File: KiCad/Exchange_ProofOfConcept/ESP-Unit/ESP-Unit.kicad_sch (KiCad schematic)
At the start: 52 parts, among them IC1 MT8870DE, J1 Jack-DC, J2 Conn_02x05_Top_Bottom, J3 Conn_01x07, U1 ESP32_NODEMCU, U2 LM317_TO-220, U3 LM358PE3, U4 TXS0108EPWR, U5 TXS0108EPWR, Y1 3.579546

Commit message: deleted:    KiCad/Exchange_ProofOfConcept/ESP-Unit/ESP-Unit-backups/ESP-Unit-2024-10-22_204833.zip 	new file:   KiCad/Exchange_ProofOfConcept/ESP-Unit/ESP-Unit-backups/ESP-Unit-2025-01-21_222447.zip 	new file:   KiCad/Exchange_ProofOfConcept/ESP-Unit/ESP-Unit-backups/ESP-Unit-2025-01-23_205217.zip 	new file:   KiCad/Exchange_ProofOfConcept/ESP-Unit/ESP-Unit-backups/ESP-Unit-2025-01-23_211741.zip 	new file:   KiCad/Exchange_ProofOfConcept/ESP-Unit/ESP-Unit-backups/ESP-Unit-2025-01-26_102636.zip 	new file:   KiCad/Exchange_ProofOfConcept/ESP-Unit/ESP-Unit-backups/ESP-Unit-2025-01-30_220613.zip 	new file:   KiCad/Exchange_ProofOfConcept/ESP-Unit/ESP-Unit-backups/ESP-Unit-2025-01-30_221846.zip 	modified:   KiCad/Exchange_ProofOfConcept/ESP-Unit/ESP-Unit.kicad_pcb 	modified:   KiCad/Exchange_ProofOfConcept/ESP-Unit/ESP-Unit.kicad_pro 	modified:   KiCad/Exchange_ProofOfConcept/ESP-Unit/ESP-Unit.kicad_sch 	modified:   KiCad/Exchange_ProofOfConcept/ESP-Unit/fp-info-cache 	deleted:    KiCad/Exchange_ProofOfConcept/Exchange_ProofOfConcept-backups/Exchange_ProofOfConcept-2024-11-20_224852.zip 	deleted:    KiCad/Exchange_ProofOfConcept/Exchange_ProofOfConcept-backups/Exchange_ProofOfConcept-2024-11-20_230009.zip 	deleted:    KiCad/Exchange_ProofOfConcept/Exchange_ProofOfConcept-backups/Exchange_ProofOfConcept-2024-11-20_231023.zip 	deleted:    KiCad/Exchange_ProofOfConcept/Exchange_ProofOfConcept-backups/Exchange_ProofOfConcept-2024-11-20_231736.zip 	new file:   KiCad/Exchange_ProofOfConcept/Exchange_ProofOfConcept-backups/Exchange_ProofOfConcept-2025-01-21_210113.zip 	new file:   KiCad/Exchange_ProofOfConcept/Exchange_ProofOfConcept-backups/Exchange_ProofOfConcept-2025-01-21_210624.zip 	new file:   KiCad/Exchange_ProofOfConcept/Exchange_ProofOfConcept-backups/Exchange_ProofOfConcept-2025-01-21_214958.zip 	new file:   KiCad/Exchange_ProofOfConcept/Exchange_ProofOfConcept-backups/Exchange_ProofOfConcept-2025-01-21_222119.zip 	deleted:    KiCad/Exchange_ProofOfConcept/Exchange_Pr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
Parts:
- removed C9: 0,1uF, Capacitor_THT:C_Disc_D5.0mm_W2.5mm_P2.50mm, symbol Device:C
- removed U4, U5: TXS0108EPWR, TSSOP-20_4.4x5mm_P0.5mm, symbol JW_library_sym:TXS0108EPWR
- added C11: 0,1uF, Capacitor_THT:C_Disc_D5.0mm_W2.5mm_P2.50mm, symbol Device:C
- added U4, U5: BOB-12009, JW_footprint_library:CONV_BOB-12009, symbol JW_library_sym:BOB-12009
- gave numbers to parts that had none: 1
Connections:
- net 3V3: now also U4.LV, U5.LV
- net 5V: now also C11.2, U4.HV, U5.HV
- net Earth: now also C11.1, U4.GND_1 (GND), U4.GND_2 (GND), U5.GND_1 (GND), U5.GND_2 (GND)
- net MCP_RESET: now also U4.HV4
- net MCP_RESET_3V: now also U4.LV4
- net Q1_3V: now also U5.LV4
- net Q2_3V: now also U5.LV3
- net Q3_3V: now also U5.LV2
- net Q4_3V: now also U5.LV1
- net SCL_3V: now also U4.LV2
- net SDA: now also U4.HV1
- net SDA_3V: now also U4.LV1
- net SLC: now also U4.HV2
- net SLIC_INT: now also U4.HV3
- net SLIC_INT_3V: now also U4.LV3
- net at IC1.11 (Q1): now also U5.HV4
- net at IC1.12 (Q2): now also U5.HV3
- net at IC1.13 (Q3): now also U5.HV2
- net at IC1.14 (Q4): now also U5.HV1
- net MT8870_PWDN: no longer names the net of IC1.6 (PWDN)
- net MT8870_PWDN_3V: no longer names the net of U1.J5_12 (G33)
- no-connect marks 30 -> 17
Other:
- moved on the sheet: C8

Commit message: modified:   KiCad/Exchange_ProofOfConcept/ESP-Unit/ESP-Unit.kicad_sch 	deleted:    KiCad/Exchange_ProofOfConcept/ESP-Unit/_autosave-ESP-Unit.kicad_sch 	modified:   include/config.h 	new file:   include/toneHandler.h 	modified:   lib/MT8816/MT8816.cpp 	modified:   src/config.cpp 	modified:   src/hookChange.cpp 	modified:   src/lineAction.cpp 	modified:   src/main.cpp 	new file:   src/toneHandler.cpp
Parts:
- removed D2: LED, LED_THT:LED_D3.0mm, symbol Device:LED
- added R?: 47K, Resistor_THT:R_Axial_DIN0207_L6.3mm_D2.5mm_P2.54mm_Vertical, symbol Device:R
- R11: value 100K -> 22K
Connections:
- net Earth: now also R?.1
- net Q1_3V: now also U1.J5_10 (G26); no longer U1.J4_14 (G0)
- net Q2_3V: now also U1.J5_13 (G32); no longer U1.J4_15 (G2)
- net STD: now reaches R11.2
- net STD: now also U1.J5_12 (G33), R?.2
- no-connect marks 17 -> 16
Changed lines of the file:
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@@
 	)
 	(junction
+		(at 156.21 128.27)
+		(diameter 0)
+		(color 0 0 0 0)
+	)
+	(junction
 		(at 39.37 170.18)
 		(diameter 0)
@@
 	)
 	(junction
-		(at 171.45 128.27)
+		(at 167.64 123.19)
 		(diameter 0)
 		(color 0 0 0 0)
@@
 	)
 	(no_connect
+		(at 38.1 125.73)
+	)
+	(no_connect
 		(at 38.1 107.95)
 	)
@@
 	)
 	(no_connect
-		(at 78.74 128.27)
-	)
-	(no_connect
 		(at 38.1 92.71)
 	)
@@
 	)
 	(no_connect
-		(at 78.74 130.81)
-	)
-	(no_connect
 		(at 269.24 151.13)
 	)
@@
 	)
 	(no_connect
+		(at 38.1 123.19)
+	)
+	(no_connect
 		(at 38.1 118.11)
 	)
@@
 		(at 78.74 92.71)
 	)
-	(no_connect
-		(at 78.74 123.19)
-	)
 	(wire
 		(pts
@@
 	(wire
 		(pts
-			(xy 160.02 123.19) (xy 158.75 123.19)
+			(xy 158.75 123.19) (xy 167.64 123.19)
 		)
 		(stroke
@@
 	(wire
 		(pts
+			(xy 167.64 128.27) (xy 167.64 123.19)
+		)
+		(stroke
+			(width 0)
+			(type default)
+		)
+	)
+	(wire
+		(pts
 			(xy 107.95 46.99) (xy 107.95 58.42)
 		)
@@
 	(wire
 		(pts
-			(xy 149.86 128.27) (xy 171.45 128.27)
+			(xy 149.86 128.27) (xy 156.21 128.27)
 		)
 		(stroke
@@
 	(wire
 		(pts
-			(xy 30.48 123.19) (xy 38.1 123.19)
-		)
-		(stroke
-			(width 0)
-			(type default)
-		)
-	)
-	(wire
-		(pts
 			(xy 39.37 175.26) (xy 39.37 177.8)
 		)
@@
 	(wire
 		(pts
-			(xy 30.48 130.81) (xy 38.1 130.81)
+			(xy 167.64 123.19) (xy 170.18 123.19)
 		)
 		(stroke
@@
 	(wire
 		(pts
-			(xy 167.64 123.19) (xy 171.45 123.19)
+			(xy 30.48 130.81) (xy 38.1 130.81)
 		)
 		(stroke
@@
 	(wire
 		(pts
+			(xy 78.74 128.27) (xy 82.55 128.27)
+		)
+		(stroke
+			(width 0)
+			(type default)
+		)
+	)
+	(wire
+		(pts
 			(xy 248.92 73.66) (xy 248.92 83.82)
 		)
@@
 	(wire
 		(pts
+			(xy 78.74 123.19) (xy 82.55 123.19)
+		)
+		(stroke
+			(width 0)
+			(type default)
+		)
+	)
+	(wire
+		(pts
 			(xy 130.81 176.53) (xy 133.35 176.53)
 		)
@@
 	(wire
 		(pts
-			(xy 171.45 128.27) (xy 171.45 138.43)
+			(xy 156.21 128.27) (xy 156.21 138.43)
 		)
 		(stroke
@@
 	(wire
 		(pts
-			(xy 171.45 123.19) (xy 171.45 128.27)
+			(xy 31.75 165.1) (xy 39.37 165.1)
 		)
 		(stroke
@@
 	(wire
 		(pts
-			(xy 31.75 165.1) (xy 39.37 165.1)
+			(xy 78.74 130.81) (xy 82.55 130.81)
 		)
 		(stroke
@@
 	(wire
 		(pts
+			(xy 156.21 128.27) (xy 160.02 128.27)
+		)
+		(stroke
+			(width 0)
+			(type default)
+		)
+	)
+	(wire
+		(pts
 			(xy 120.65 110.49) (xy 124.46 110.49)
 		)
@@
 	(wire
 		(pts
-			(xy 30.48 125.73) (xy 38.1 125.73)
-		)
-		(stroke
-			(width 0)
-			(type default)
-		)
-	)
-	(wire
-		(pts
 			(xy 74.93 50.8) (xy 83.82 50.8)
 		)
@@
 		)
 	)
+	(label "STD"
+		(at 82.55 130.81 0)
+		(effects
+			(font
+				(size 1.27 1.27)
+			)
+			(justify left bottom)
+		)
+	)
 	(label "3V3"
 		(at 92.71 85.09 0)
@@
 		)
 	)
+	(label "STD"
+		(at 170.18 123.19 0)
+		(effects
+			(font
+				(size 1.27 1.27)
+			)
+			(justify left bottom)
+		)
+	)
 	(label "5V"
 		(at 118.11 86.36 180)
@@
 		)
 	)
-	(label "Q2_3V"
-		(at 30.48 125.73 180)
-		(effects
-			(font
-				(size 1.27 1.27)
-			)
-			(justify right bottom)
-		)
-	)
 	(label "Audio_SLIC-Amp"
 		(at 81.28 167.64 0)
@@
 		)
 	)
+	(label "Q1_3V"
+		(at 82.55 123.19 0)
+		(effects
+			(font
+				(size 1.27 1.27)
+			)
+			(justify left bottom)
+		)
+	)
 	(label "3V3"
 		(at 180.34 55.88 0)
@@
 		)
 	)
+	(label "Q2_3V"
+		(at 82.55 128.27 0)
+		(effects
+			(font
+				(size 1.27 1.27)
+			)
+			(justify left bottom)
+		)
+	)
 	(label "Audio_SLIC"
 		(at 248.92 71.12 0)
@@
 		)
 	)
-	(label "Q1_3V"
-		(at 30.48 123.19 180)
-		(effects
-			(font
-				(size 1.27 1.27)
-			)
-			(justify right bottom)
-		)
-	)
 	(label "Vref"
 		(at 134.62 31.75 0)
@@
 	)
 	(symbol
+		(lib_id "Device:R")
+		(at 163.83 128.27 90)
+		(unit 1)
+		(exclude_from_sim no)
+		(in_bom yes)
+		(on_board yes)
+		(dnp no)
+		(property "Reference" "R?"
+			(at 166.624 130.302 90)
+			(effects
+				(font
+					(size 1.27 1.27)
+				)
+				(justify left)
+			)
+		)
+		(property "Value" "47K"
+			(at 166.37 128.27 90)
+			(effects
+				(font
+					(size 1.27 1.27)
+				)
+				(justify left)
+			)
+		)
+		(property "Footprint" "Resistor_THT:R_Axial_DIN0207_L6.3mm_D2.5mm_P2.54mm_Vertical"
+			(at 163.83 130.048 90)
+			(effects
+				(font
+					(size 1.27 1.27)
+				)
+				(hide yes)
+			)
+		)
+		(property "Datasheet" "~"
+			(at 163.83 128.27 0)
+			(effects
+				(font
+					(size 1.27 1.27)
+				)
+				(hide yes)
+			)
+		)
+		(property "Description" "Resistor"
+			(at 163.83 128.27 0)
+			(effects
+				(font
+					(size 1.27 1.27)
+				)
+				(hide yes)
+			)
+		)
+		(pin "2"
+		)
+		(pin "1"
+		)
+		(instances
+			(project "ESP-Unit"
+				(path "/2411d7b8-ed2d-41a6-b5ea-3554d7cee414"
+					(reference "R?")
+					(unit 1)
+				)
+			)
+		)
+	)
+	(symbol
 		(lib_id "Device:C_Polarized_US")
 		(at 30.48 85.09 0)
@@
 	(symbol
 		(lib_id "power:Earth")
-		(at 171.45 138.43 0)
+		(at 156.21 138.43 0)
 		(mirror y)
 		(unit 1)
@@
 		(fields_autoplaced yes)
 		(property "Reference" "#PWR08"
-			(at 171.45 144.78 0)
+			(at 156.21 144.78 0)
 			(effects
 				(font
@@
 		)
 		(property "Value" "Earth"
-			(at 171.45 143.51 0)
+			(at 156.21 143.51 0)
 			(effects
 				(font
@@
 		)
 		(property "Footprint" ""
-			(at 171.45 138.43 0)
+			(at 156.21 138.43 0)
 			(effects
 				(font
@@
 		)
 		(property "Datasheet" "~"
-			(at 171.45 138.43 0)
+			(at 156.21 138.43 0)
 			(effects
 				(font
@@
 		)
 		(property "Description" "Power symbol creates a global label with name \"Earth\""
-			(at 171.45 138.43 0)
+			(at 156.21 138.43 0)
 			(effects
 				(font
@@
 	)
 	(symbol
-		(lib_id "Device:LED")
-		(at 163.83 123.19 180)
-		(unit 1)
-		(exclude_from_sim no)
-		(in_bom yes)
-		(on_board yes)
-		(dnp no)
-		(property "Reference" "D2"
-			(at 163.322 120.396 0)
-			(effects
-				(font
-					(size 1.27 1.27)
-				)
-			)
-		)
-		(property "Value" "LED"
-			(at 163.83 125.984 0)
-			(effects
-				(font
-					(size 1.27 1.27)
-				)
-			)
-		)
-		(property "Footprint" "LED_THT:LED_D3.0mm"
-			(at 163.83 123.19 0)
-			(effects
-				(font
-					(size 1.27 1.27)
-				)
-				(hide yes)
-			)
-		)
-		(property "Datasheet" "~"
-			(at 163.83 123.19 0)
-			(effects
-				(font
-					(size 1.27 1.27)
-				)
-				(hide yes)
-			)
-		)
-		(property "Description" "Light emitting diode"
-			(at 163.83 123.19 0)
-			(effects
-				(font
-					(size 1.27 1.27)
-				)
-				(hide yes)
-			)
-		)
-		(pin "1"
-		)
-		(pin "2"
-		)
-		(instances
-			(project "ESP-Unit"
-				(path "/2411d7b8-ed2d-41a6-b5ea-3554d7cee414"
-					(reference "D2")
-					(unit 1)
-				)
-			)
-		)
-	)
-	(symbol
 		(lib_id "Device:R")
 		(at 154.94 123.19 90)
@@
 			)
 		)
-		(property "Value" "100K"
+		(property "Value" "22K"
 			(at 157.48 123.19 90)
 			(effects

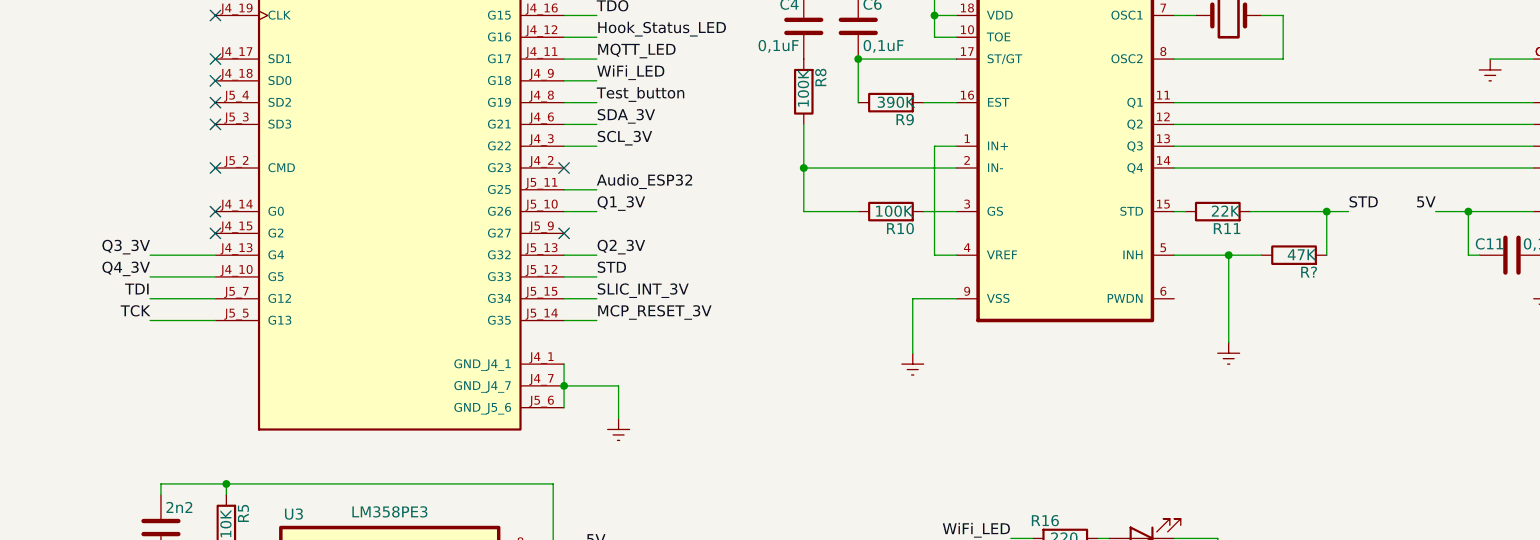
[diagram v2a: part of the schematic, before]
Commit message: Revert "Number dailing"
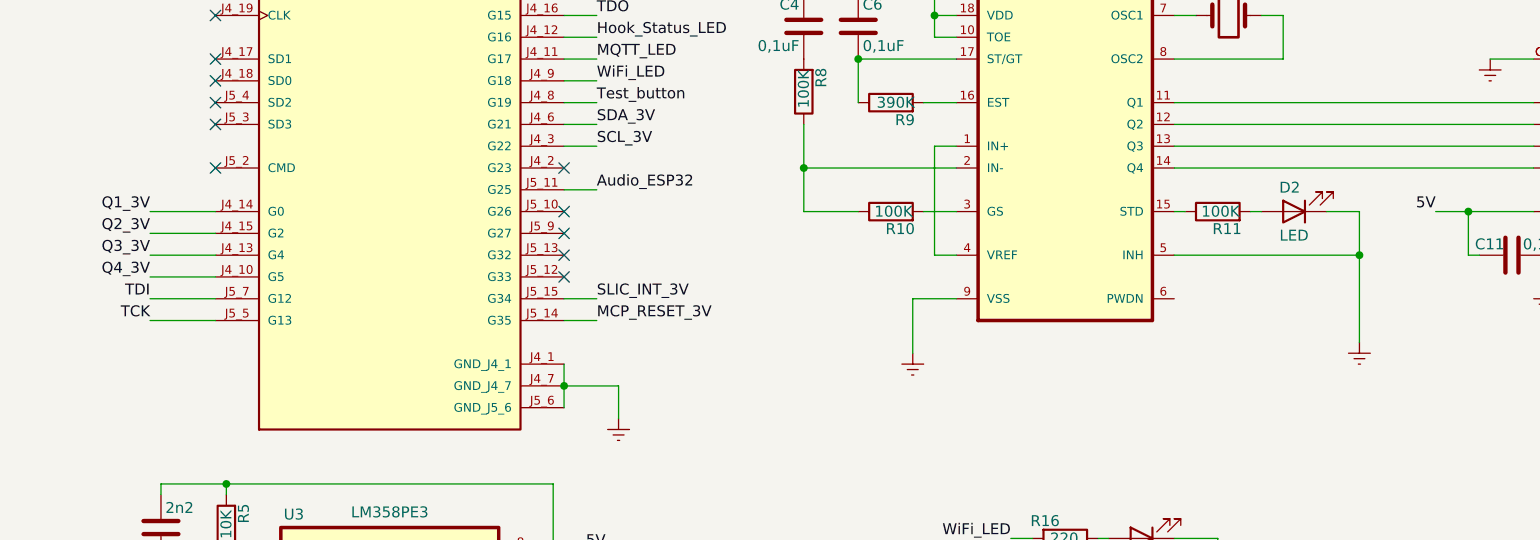
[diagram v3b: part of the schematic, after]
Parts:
- removed R?: 47K, Resistor_THT:R_Axial_DIN0207_L6.3mm_D2.5mm_P2.54mm_Vertical, symbol Device:R
- added D2: LED, LED_THT:LED_D3.0mm, symbol Device:LED
- R11: value 22K -> 100K
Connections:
- net Earth: now also D2.1 (K)
- net Q1_3V: now also U1.J4_14 (G0); no longer U1.J5_10 (G26)
- net Q2_3V: now also U1.J4_15 (G2); no longer U1.J5_13 (G32)
- net STD: no longer names the net of R11.2
- net STD: now also D2.2 (A); no longer U1.J5_12 (G33)
- no-connect marks 16 -> 17
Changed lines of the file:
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@@
 	)
 	(junction
-		(at 156.21 128.27)
-		(diameter 0)
-		(color 0 0 0 0)
-	)
-	(junction
 		(at 39.37 170.18)
 		(diameter 0)
@@
 	)
 	(junction
-		(at 167.64 123.19)
+		(at 171.45 128.27)
 		(diameter 0)
 		(color 0 0 0 0)
@@
 	)
 	(no_connect
-		(at 38.1 125.73)
-	)
-	(no_connect
 		(at 38.1 107.95)
 	)
@@
 	)
 	(no_connect
+		(at 78.74 128.27)
+	)
+	(no_connect
 		(at 38.1 92.71)
 	)
@@
 	)
 	(no_connect
+		(at 78.74 130.81)
+	)
+	(no_connect
 		(at 269.24 151.13)
 	)
@@
 	)
 	(no_connect
-		(at 38.1 123.19)
-	)
-	(no_connect
 		(at 38.1 118.11)
 	)
@@
 		(at 78.74 92.71)
 	)
+	(no_connect
+		(at 78.74 123.19)
+	)
 	(wire
 		(pts
@@
 	(wire
 		(pts
-			(xy 158.75 123.19) (xy 167.64 123.19)
+			(xy 160.02 123.19) (xy 158.75 123.19)
 		)
 		(stroke
@@
 	(wire
 		(pts
-			(xy 167.64 128.27) (xy 167.64 123.19)
-		)
-		(stroke
-			(width 0)
-			(type default)
-		)
-	)
-	(wire
-		(pts
 			(xy 107.95 46.99) (xy 107.95 58.42)
 		)
@@
 	(wire
 		(pts
-			(xy 149.86 128.27) (xy 156.21 128.27)
+			(xy 149.86 128.27) (xy 171.45 128.27)
 		)
 		(stroke
@@
 	(wire
 		(pts
+			(xy 30.48 123.19) (xy 38.1 123.19)
+		)
+		(stroke
+			(width 0)
+			(type default)
+		)
+	)
+	(wire
+		(pts
 			(xy 39.37 175.26) (xy 39.37 177.8)
 		)
@@
 	(wire
 		(pts
-			(xy 167.64 123.19) (xy 170.18 123.19)
+			(xy 30.48 130.81) (xy 38.1 130.81)
 		)
 		(stroke
@@
 	(wire
 		(pts
-			(xy 30.48 130.81) (xy 38.1 130.81)
+			(xy 167.64 123.19) (xy 171.45 123.19)
 		)
 		(stroke
@@
 	(wire
 		(pts
-			(xy 78.74 128.27) (xy 82.55 128.27)
-		)
-		(stroke
-			(width 0)
-			(type default)
-		)
-	)
-	(wire
-		(pts
 			(xy 248.92 73.66) (xy 248.92 83.82)
 		)
@@
 	(wire
 		(pts
-			(xy 78.74 123.19) (xy 82.55 123.19)
-		)
-		(stroke
-			(width 0)
-			(type default)
-		)
-	)
-	(wire
-		(pts
 			(xy 130.81 176.53) (xy 133.35 176.53)
 		)
@@
 	(wire
 		(pts
-			(xy 156.21 128.27) (xy 156.21 138.43)
+			(xy 171.45 128.27) (xy 171.45 138.43)
 		)
 		(stroke
@@
 	(wire
 		(pts
-			(xy 31.75 165.1) (xy 39.37 165.1)
+			(xy 171.45 123.19) (xy 171.45 128.27)
 		)
 		(stroke
@@
 	(wire
 		(pts
-			(xy 78.74 130.81) (xy 82.55 130.81)
+			(xy 31.75 165.1) (xy 39.37 165.1)
 		)
 		(stroke
@@
 	(wire
 		(pts
-			(xy 156.21 128.27) (xy 160.02 128.27)
-		)
-		(stroke
-			(width 0)
-			(type default)
-		)
-	)
-	(wire
-		(pts
 			(xy 120.65 110.49) (xy 124.46 110.49)
 		)
@@
 	(wire
 		(pts
+			(xy 30.48 125.73) (xy 38.1 125.73)
+		)
+		(stroke
+			(width 0)
+			(type default)
+		)
+	)
+	(wire
+		(pts
 			(xy 74.93 50.8) (xy 83.82 50.8)
 		)
@@
 		)
 	)
-	(label "STD"
-		(at 82.55 130.81 0)
-		(effects
-			(font
-				(size 1.27 1.27)
-			)
-			(justify left bottom)
-		)
-	)
 	(label "3V3"
 		(at 92.71 85.09 0)
@@
 		)
 	)
-	(label "STD"
-		(at 170.18 123.19 0)
-		(effects
-			(font
-				(size 1.27 1.27)
-			)
-			(justify left bottom)
-		)
-	)
 	(label "5V"
 		(at 118.11 86.36 180)
@@
 		)
 	)
+	(label "Q2_3V"
+		(at 30.48 125.73 180)
+		(effects
+			(font
+				(size 1.27 1.27)
+			)
+			(justify right bottom)
+		)
+	)
 	(label "Audio_SLIC-Amp"
 		(at 81.28 167.64 0)
@@
 		)
 	)
-	(label "Q1_3V"
-		(at 82.55 123.19 0)
-		(effects
-			(font
-				(size 1.27 1.27)
-			)
-			(justify left bottom)
-		)
-	)
 	(label "3V3"
 		(at 180.34 55.88 0)
@@
 		)
 	)
-	(label "Q2_3V"
-		(at 82.55 128.27 0)
-		(effects
-			(font
-				(size 1.27 1.27)
-			)
-			(justify left bottom)
-		)
-	)
 	(label "Audio_SLIC"
 		(at 248.92 71.12 0)
@@
 		)
 	)
+	(label "Q1_3V"
+		(at 30.48 123.19 180)
+		(effects
+			(font
+				(size 1.27 1.27)
+			)
+			(justify right bottom)
+		)
+	)
 	(label "Vref"
 		(at 134.62 31.75 0)
@@
 	)
 	(symbol
-		(lib_id "Device:R")
-		(at 163.83 128.27 90)
-		(unit 1)
-		(exclude_from_sim no)
-		(in_bom yes)
-		(on_board yes)
-		(dnp no)
-		(property "Reference" "R?"
-			(at 166.624 130.302 90)
-			(effects
-				(font
-					(size 1.27 1.27)
-				)
-				(justify left)
-			)
-		)
-		(property "Value" "47K"
-			(at 166.37 128.27 90)
-			(effects
-				(font
-					(size 1.27 1.27)
-				)
-				(justify left)
-			)
-		)
-		(property "Footprint" "Resistor_THT:R_Axial_DIN0207_L6.3mm_D2.5mm_P2.54mm_Vertical"
-			(at 163.83 130.048 90)
-			(effects
-				(font
-					(size 1.27 1.27)
-				)
-				(hide yes)
-			)
-		)
-		(property "Datasheet" "~"
-			(at 163.83 128.27 0)
-			(effects
-				(font
-					(size 1.27 1.27)
-				)
-				(hide yes)
-			)
-		)
-		(property "Description" "Resistor"
-			(at 163.83 128.27 0)
-			(effects
-				(font
-					(size 1.27 1.27)
-				)
-				(hide yes)
-			)
-		)
-		(pin "2"
-		)
-		(pin "1"
-		)
-		(instances
-			(project "ESP-Unit"
-				(path "/2411d7b8-ed2d-41a6-b5ea-3554d7cee414"
-					(reference "R?")
-					(unit 1)
-				)
-			)
-		)
-	)
-	(symbol
 		(lib_id "Device:C_Polarized_US")
 		(at 30.48 85.09 0)
@@
 	(symbol
 		(lib_id "power:Earth")
-		(at 156.21 138.43 0)
+		(at 171.45 138.43 0)
 		(mirror y)
 		(unit 1)
@@
 		(fields_autoplaced yes)
 		(property "Reference" "#PWR08"
-			(at 156.21 144.78 0)
+			(at 171.45 144.78 0)
 			(effects
 				(font
@@
 		)
 		(property "Value" "Earth"
-			(at 156.21 143.51 0)
+			(at 171.45 143.51 0)
 			(effects
 				(font
@@
 		)
 		(property "Footprint" ""
-			(at 156.21 138.43 0)
+			(at 171.45 138.43 0)
 			(effects
 				(font
@@
 		)
 		(property "Datasheet" "~"
-			(at 156.21 138.43 0)
+			(at 171.45 138.43 0)
 			(effects
 				(font
@@
 		)
 		(property "Description" "Power symbol creates a global label with name \"Earth\""
-			(at 156.21 138.43 0)
+			(at 171.45 138.43 0)
 			(effects
 				(font
@@
 	)
 	(symbol
+		(lib_id "Device:LED")
+		(at 163.83 123.19 180)
+		(unit 1)
+		(exclude_from_sim no)
+		(in_bom yes)
+		(on_board yes)
+		(dnp no)
+		(property "Reference" "D2"
+			(at 163.322 120.396 0)
+			(effects
+				(font
+					(size 1.27 1.27)
+				)
+			)
+		)
+		(property "Value" "LED"
+			(at 163.83 125.984 0)
+			(effects
+				(font
+					(size 1.27 1.27)
+				)
+			)
+		)
+		(property "Footprint" "LED_THT:LED_D3.0mm"
+			(at 163.83 123.19 0)
+			(effects
+				(font
+					(size 1.27 1.27)
+				)
+				(hide yes)
+			)
+		)
+		(property "Datasheet" "~"
+			(at 163.83 123.19 0)
+			(effects
+				(font
+					(size 1.27 1.27)
+				)
+				(hide yes)
+			)
+		)
+		(property "Description" "Light emitting diode"
+			(at 163.83 123.19 0)
+			(effects
+				(font
+					(size 1.27 1.27)
+				)
+				(hide yes)
+			)
+		)
+		(pin "1"
+		)
+		(pin "2"
+		)
+		(instances
+			(project "ESP-Unit"
+				(path "/2411d7b8-ed2d-41a6-b5ea-3554d7cee414"
+					(reference "D2")
+					(unit 1)
+				)
+			)
+		)
+	)
+	(symbol
 		(lib_id "Device:R")
 		(at 154.94 123.19 90)
@@
 			)
 		)
-		(property "Value" "22K"
+		(property "Value" "100K"
 			(at 157.48 123.19 90)
 			(effects
